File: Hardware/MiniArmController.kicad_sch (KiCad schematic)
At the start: 2 parts, among them U1 Teensy4.1_DEV-16771

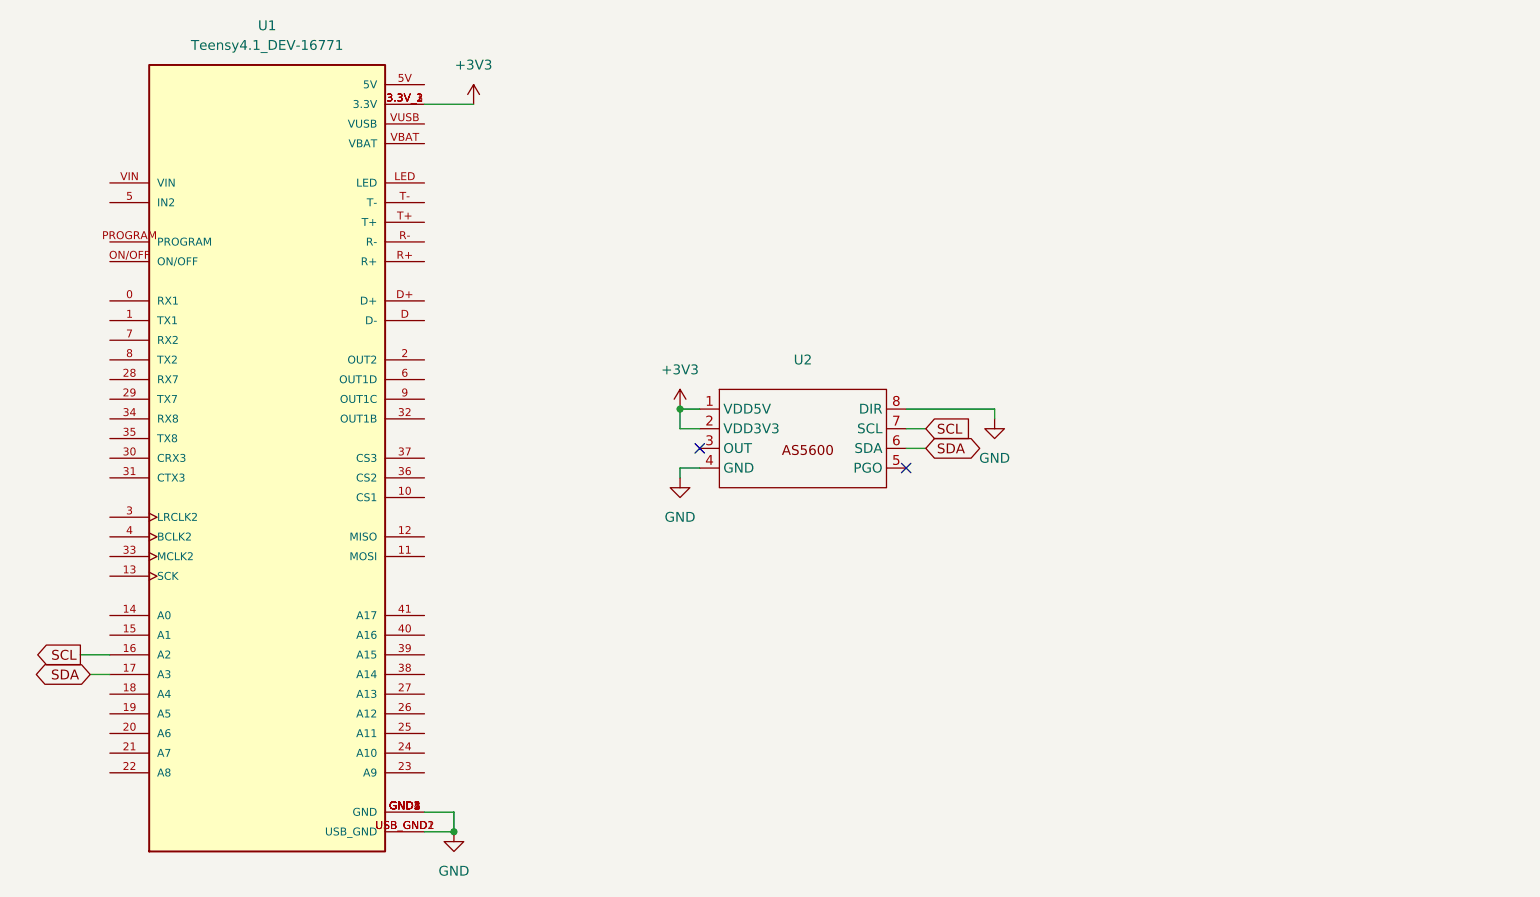
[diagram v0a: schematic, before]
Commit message: Add two 3215BLCD motors
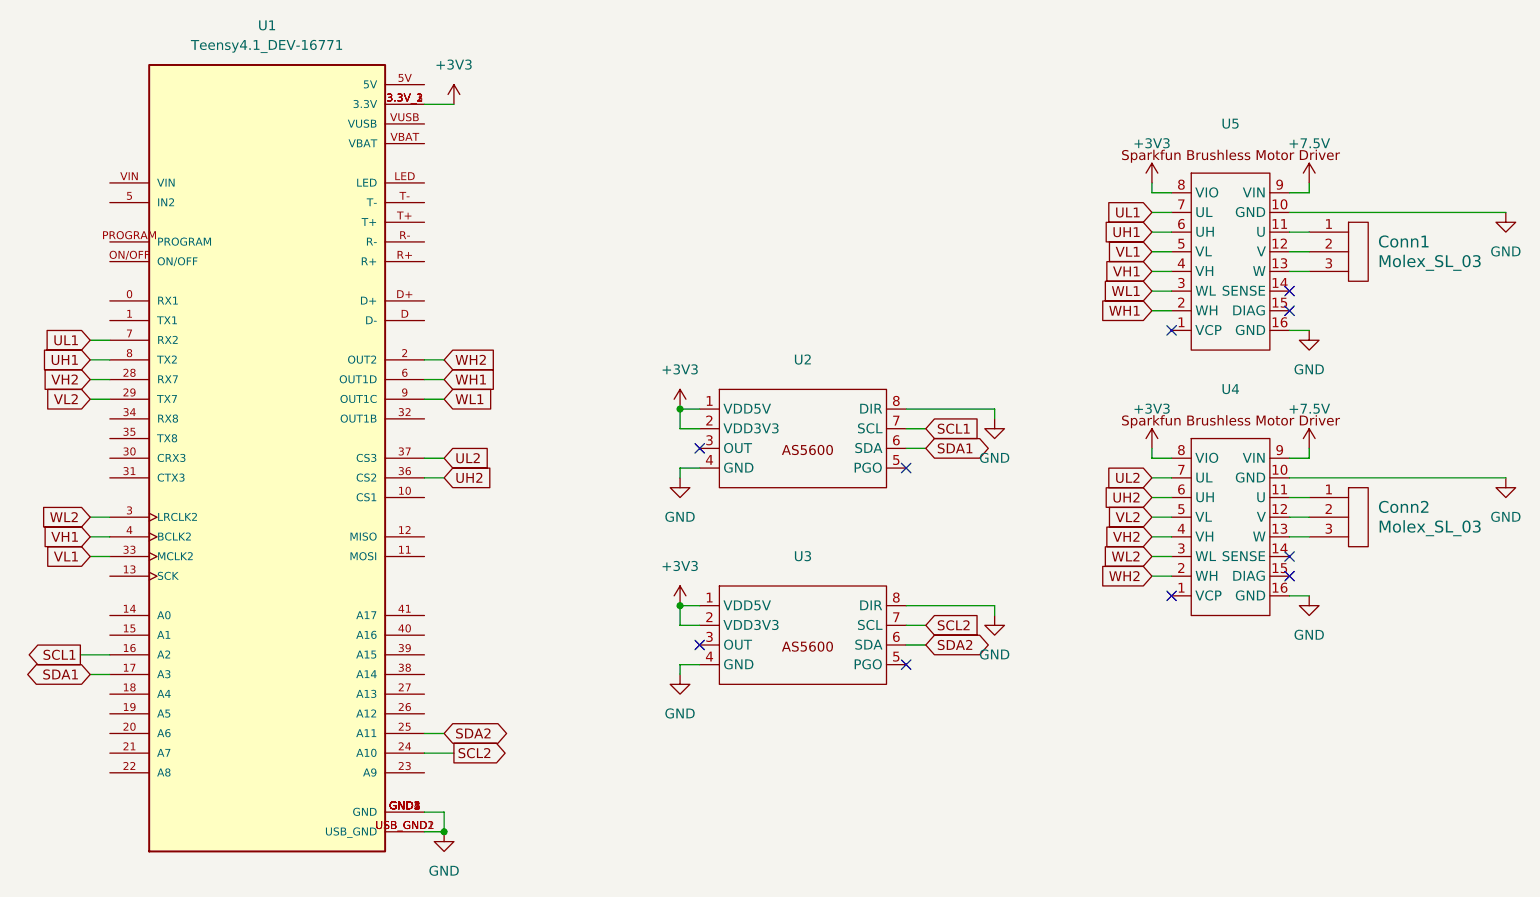
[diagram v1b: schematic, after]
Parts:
- added Conn1, Conn2: Molex_SL_03, symbol MRDT_Connectors:Molex_SL_03
- added U3: ~, Package_SO:SOIC-8_3.9x4.9mm_P1.27mm, symbol MRDT_Sensors:AS5600
- added U4, U5: ~, symbol MiniArmController:Brushless_Motor_Driver
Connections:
- net +3V3: now also U3.1 (VDD5V), U3.2 (VDD3V3), U4.8 (VIO), U5.8 (VIO)
- net GND: now also U3.4 (GND), U3.8 (DIR), U4.10 (GND), U4.16 (GND), U5.10 (GND), U5.16 (GND)
- net WH2: now reaches U1.2 (OUT2)
- net WH2: now also U4.2 (WH)
- net SCL2: now reaches U1.24 (A10)
- net SCL2: now also U3.7 (SCL)
- net SDA2: now reaches U1.25 (A11)
- net SDA2: now also U3.6 (SDA)
- net VH2: now reaches U1.28 (RX7)
- net VH2: now also U4.4 (VH)
- net VL2: now reaches U1.29 (TX7)
- net VL2: now also U4.5 (VL)
- net WL2: now reaches U1.3 (LRCLK2)
- net WL2: now also U4.3 (WL)
- net VL1: now reaches U1.33 (MCLK2)
- net VL1: now also U5.5 (VL)
- net UH2: now reaches U1.36 (CS2)
- net UH2: now also U4.6 (UH)
- net UL2: now reaches U1.37 (CS3)
- net UL2: now also U4.7 (UL)
- net VH1: now reaches U1.4 (BCLK2)
- net VH1: now also U5.4 (VH)
- net WH1: now reaches U1.6 (OUT1D)
- net WH1: now also U5.2 (WH)
- net UL1: now reaches U1.7 (RX2)
- net UL1: now also U5.7 (UL)
- net UH1: now reaches U1.8 (TX2)
- net UH1: now also U5.6 (UH)
- net WL1: now reaches U1.9 (OUT1C)
- net WL1: now also U5.3 (WL)
- net SCL renamed SCL1
- net SDA renamed SDA1
- new net: Conn2.1, U4.11 (U)
- new net: Conn2.2, U4.12 (V)
- new net: Conn2.3, U4.13 (W)
- new net: Conn1.1, U5.11 (U)
- new net: Conn1.2, U5.12 (V)
- new net: Conn1.3, U5.13 (W)
- new net +7.5V: U4.9 (VIN), U5.9 (VIN)
- no-connect marks 2 -> 10

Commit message: Superseded changes
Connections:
- net VH2: now also U1.29 (TX7); no longer U1.28 (RX7)
- net VL2: now also U1.28 (RX7); no longer U1.29 (TX7)
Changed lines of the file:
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@@
+	(wire
+		(pts
+			(xy 53.34 74.93) (xy 55.88 74.93)
+		)
+		(stroke
+			(width 0)
+			(type default)
+		)
+	)
 	(wire
 		(pts
@@
 	(wire
 		(pts
-			(xy 53.34 74.93) (xy 55.88 74.93)
-		)
-		(stroke
-			(width 0)
-			(type default)
-		)
-	)
-	(wire
-		(pts
 			(xy 190.5 92.71) (xy 193.04 92.71)
 		)
@@
 	(wire
 		(pts
+			(xy 53.34 77.47) (xy 55.88 77.47)
+		)
+		(stroke
+			(width 0)
+			(type default)
+		)
+	)
+	(wire
+		(pts
 			(xy 190.5 55.88) (xy 193.04 55.88)
 		)
@@
 		(pts
 			(xy 210.82 60.96) (xy 208.28 60.96)
-		)
-		(stroke
-			(width 0)
-			(type default)
-		)
-	)
-	(wire
-		(pts
-			(xy 53.34 77.47) (xy 55.88 77.47)
 		)
 		(stroke
@@
 	(global_label "VH2"
 		(shape input)
-		(at 53.34 74.93 180)
+		(at 53.34 77.47 180)
 		(fields_autoplaced yes)
 		(effects
@@
 		)
 		(property "Intersheetrefs" "${INTERSHEET_REFS}"
-			(at 46.7262 74.93 0)
+			(at 46.7262 77.47 0)
 			(effects
 				(font
@@
 	(global_label "VL2"
 		(shape input)
-		(at 53.34 77.47 180)
+		(at 53.34 74.93 180)
 		(fields_autoplaced yes)
 		(effects
@@
 		)
 		(property "Intersheetrefs" "${INTERSHEET_REFS}"
-			(at 47.0286 77.47 0)
+			(at 47.0286 74.93 0)
 			(effects
 				(font
